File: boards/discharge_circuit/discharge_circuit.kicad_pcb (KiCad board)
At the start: 2 copper layers, 93 x 43.5 mm, 11 parts, among them J1 Unfused TS, J2 Shutdown Circuit, J3 TSMP/TSAL, K1 G2RL-1-E

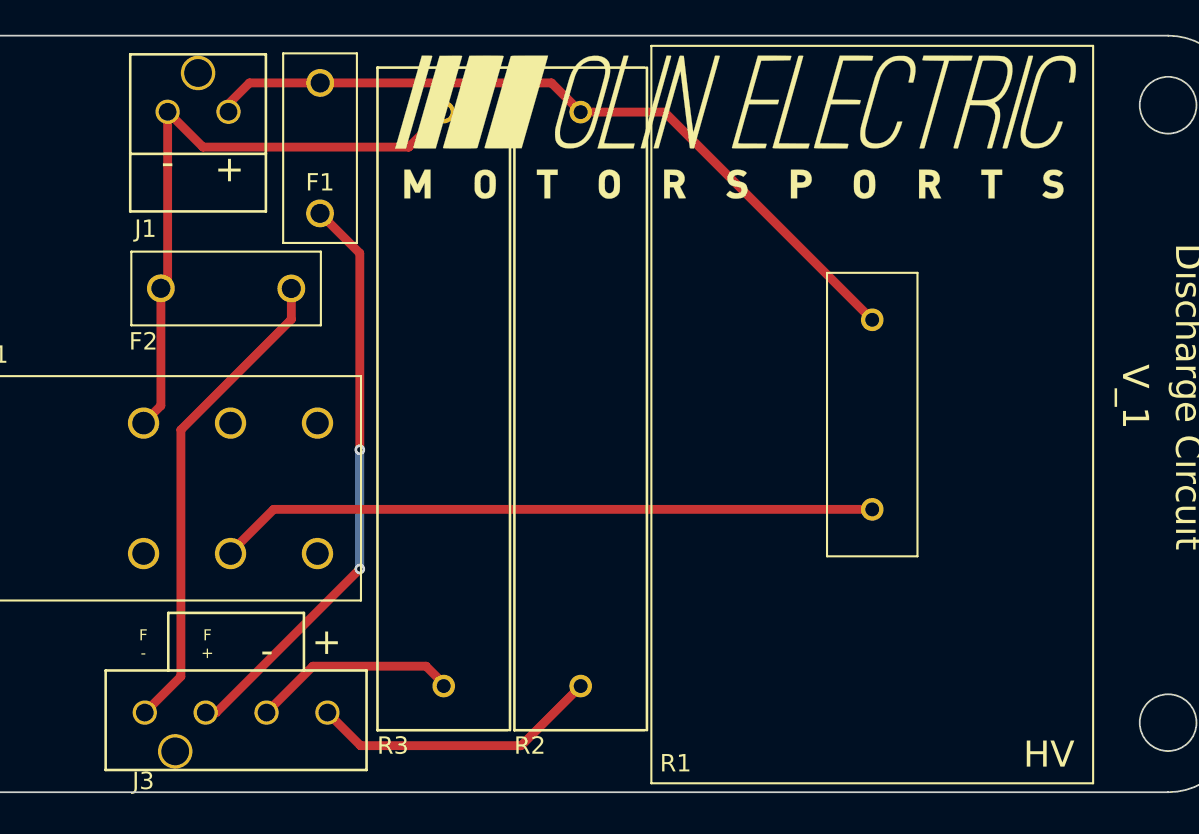
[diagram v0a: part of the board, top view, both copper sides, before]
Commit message: modifying discharge circuit to fit in accumulator
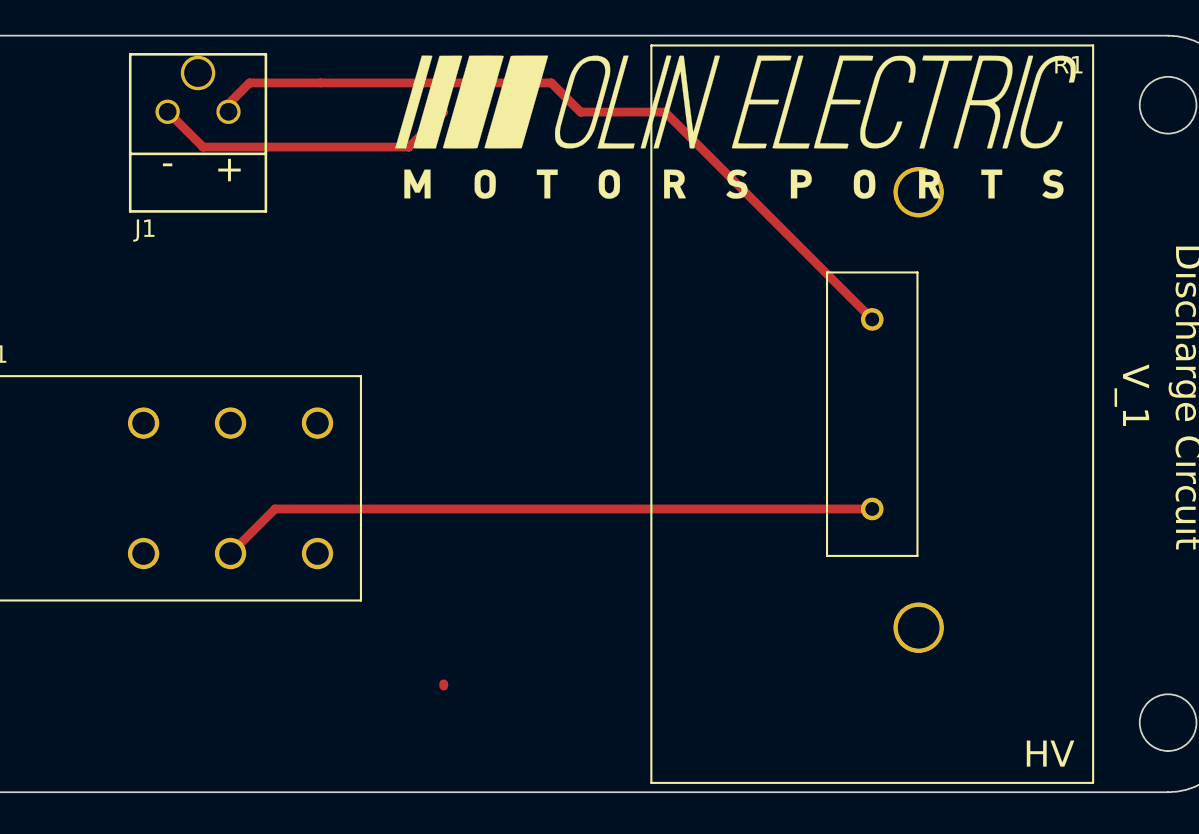
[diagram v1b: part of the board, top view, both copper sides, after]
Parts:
- removed F1, F2: F_3.15A_450V, footprints:Fuse_TE7_Littelfuse-807Series
- removed J3: TSMP/TSAL, footprints:Ultrafit_4
- removed R2, R3: R_10k_HV, footprints:R_10K_HV
- moved R1 10.9 mm to (174.0, 99.6), turned to 270 degrees
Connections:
- R1 pad 1: Net-(K1-Pad6) -> /TS+Unfused
- R1 pad 2: /TS+Unfused -> Net-(K1-Pad6)
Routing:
- net /TS+Fused: track 33.7 -> 0.00 mm, vias 2 -> 0
- net /TS-Fused: track 27.9 -> 0.00 mm
- net /TS-Unfused: track 36.6 -> 17.6 mm
- net Net-(J3-Pad4): track 16.8 -> 0.00 mm
- net Net-(J3-Pad3): track 11.8 -> 0.00 mm
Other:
- board text removed: "F +"
- board text removed: "F -"

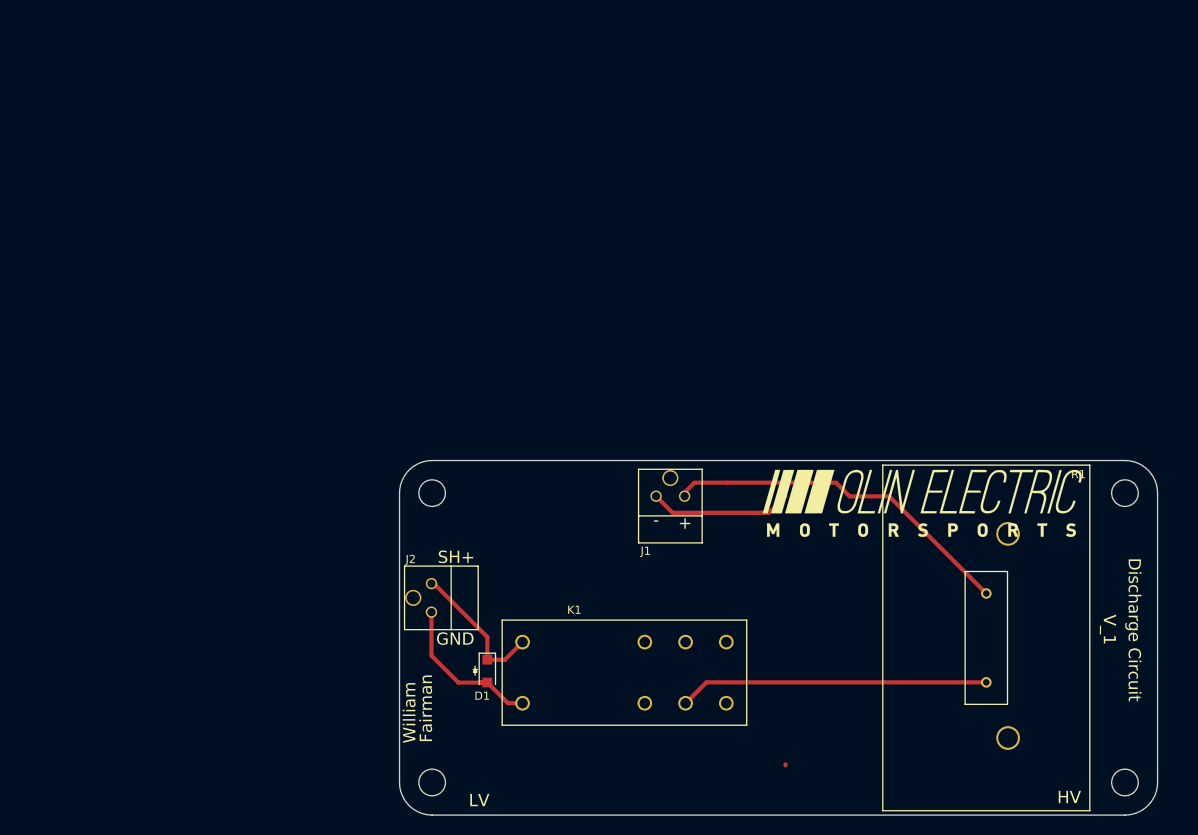
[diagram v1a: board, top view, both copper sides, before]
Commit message: restored older version of discharge circuit and added additional connectors
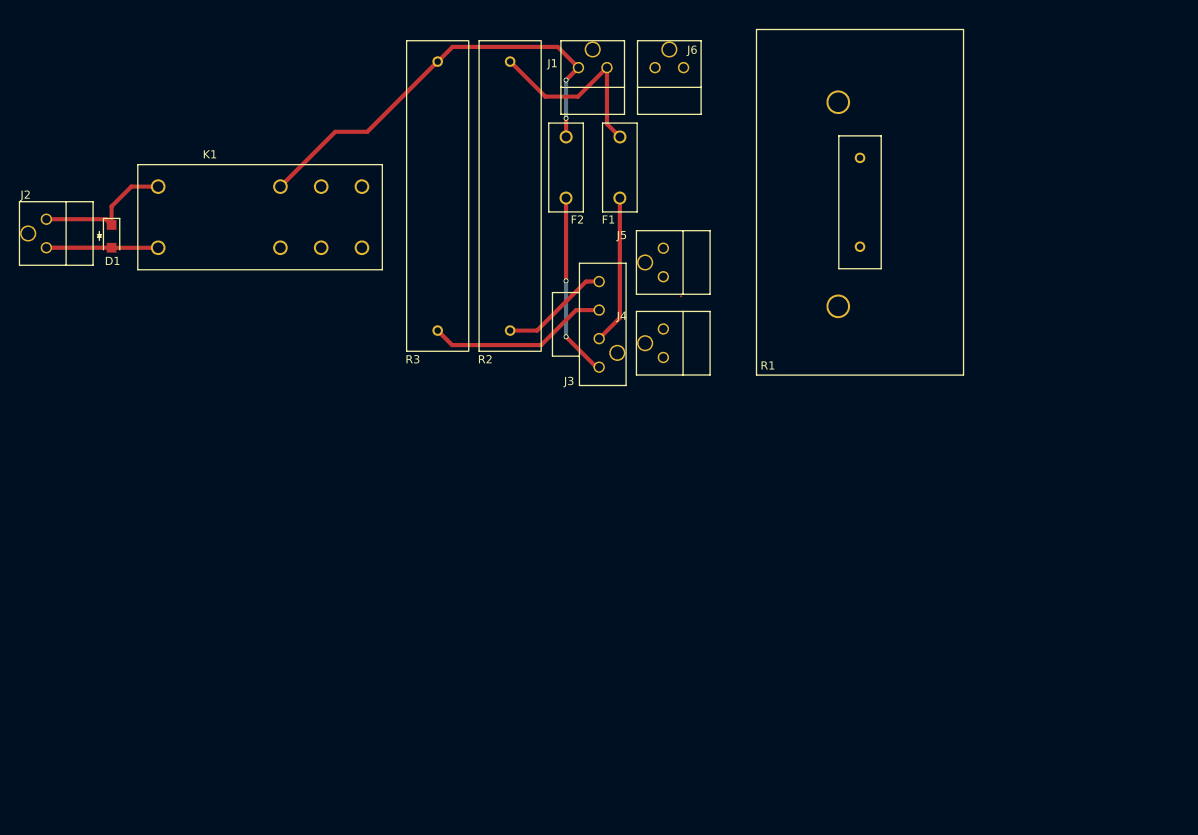
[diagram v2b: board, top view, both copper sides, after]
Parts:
- removed G***: LOGO, footprints:Logo_Large
- added F1: F_3.15A_450V, footprints:Fuse_TE7_Littelfuse-807Series, F.Cu at (129.0, 51.1)
- added F2: F_3.15A_450V, footprints:Fuse_TE7_Littelfuse-807Series, F.Cu at (122.4, 51.1)
- added J3: TSMP, footprints:Ultrafit_4, F.Cu at (126.5, 66.5)
- added J4: TSAL, footprints:Ultrafit_2, F.Cu at (134.4, 70.6)
- added J5: IMD, footprints:Ultrafit_2, F.Cu at (134.4, 60.7)
- added J6: EM/Precharge, footprints:Ultrafit_2, F.Cu at (133.3, 35.1)
- added R2: R_10k_HV, footprints:R_10K_HV, F.Cu at (115.6, 67.3)
- added R3: R_10k_HV, footprints:R_10K_HV, F.Cu at (106.7, 67.3)
- moved K1 71.6 mm to (72.4, 57.1)
- moved D1 70.5 mm to (66.7, 55.8)
- moved J2 65.0 mm to (58.7, 57.1)
- moved J1 53.4 mm to (124.0, 35.1)
- moved R1 45.3 mm to (158.5, 57.0), turned to 90 degrees
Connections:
- R1 pad 1: /TS+Unfused -> Net-(K1-Pad6)
- R1 pad 2: Net-(K1-Pad6) -> /TS+Unfused
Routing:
- net Net-(K1-Pad6): track 38.0 -> 0.00 mm
- net /TS-Unfused: track 17.6 -> 53.9 mm, vias 0 -> 2
- net Net-(J3-Pad3): track 0.00 -> 19.8 mm
- net /TS+Unfused: track 43.8 -> 24.3 mm
- net /TS-Fused: track 0.00 -> 17.0 mm, vias 0 -> 2
- net /TS+Fused: track 0.00 -> 14.7 mm
- net Net-(J3-Pad4): track 0.00 -> 10.1 mm
- net Net-(J3-Pad1): track 0.00 -> 8.91 mm
- net Net-(J3-Pad2): track 0.00 -> 6.11 mm
- net GND: track 19.7 -> 13.7 mm
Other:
- board outline removed
- net class Default: clearance 0.1016 -> 0.0508; via_dia 0.6096 -> 0.6; via_drill 0.3048 -> 0.4
- rule trace_clearance: 0.1016 -> 0.0508
- rule via_min_drill: 0.3048 -> 0.3
- rule via_min_size: 0.6096 -> 0.4
- board text removed: "+"
- board text removed: "-"
- board text removed: "Discharge Circuit"
- board text removed: "Fairman"
- board text removed: "GND"
- board text removed: "HV"
- board text removed: "LV"
- board text removed: "SH+"
- board text removed: "V_1"
- board text removed: "William"

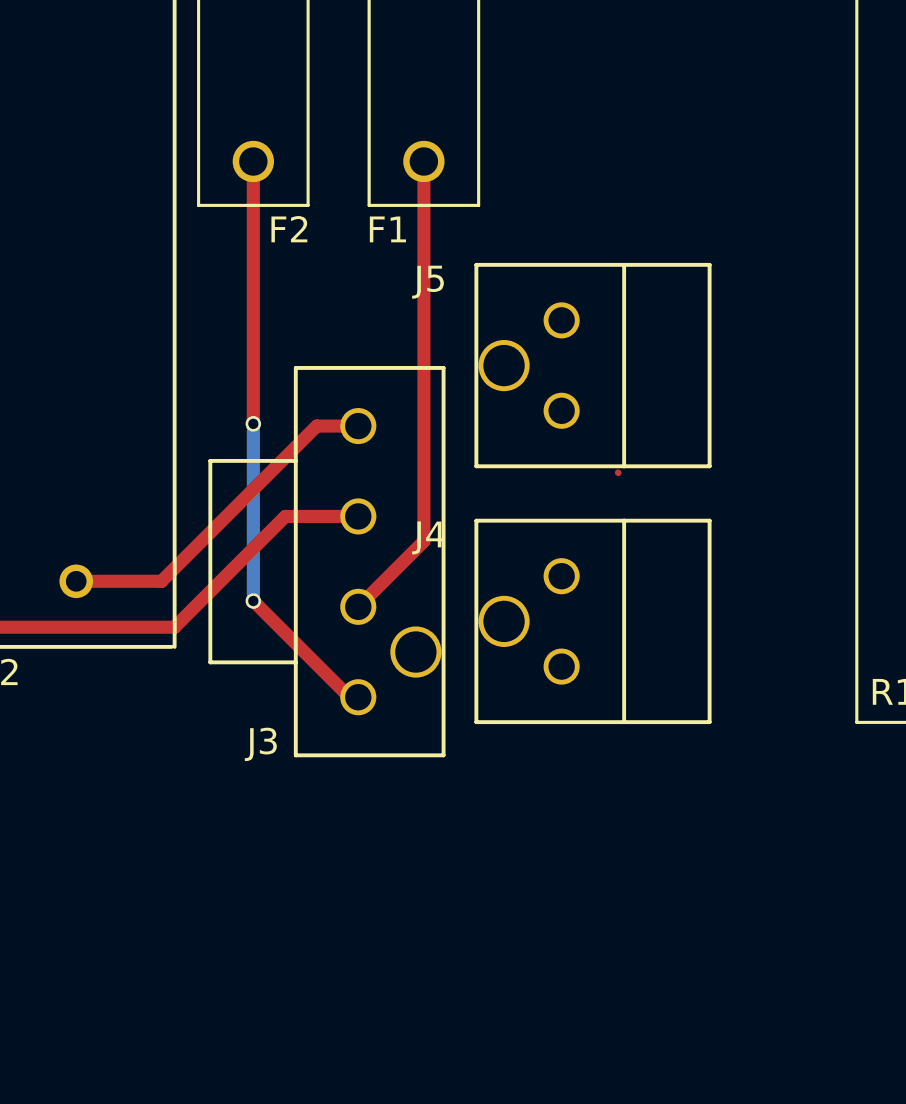
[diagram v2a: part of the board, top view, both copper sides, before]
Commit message: modified discharge circuit
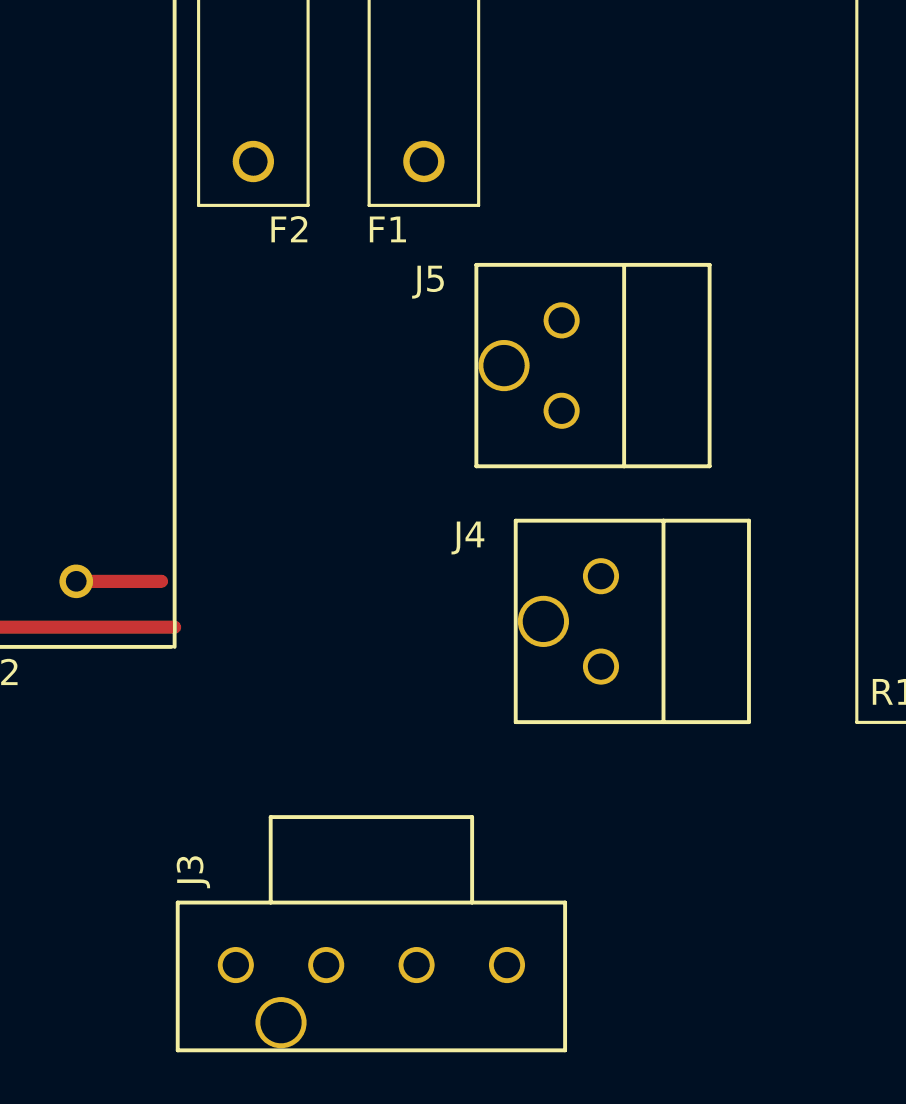
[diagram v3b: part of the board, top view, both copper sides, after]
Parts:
- moved J3 15.6 mm to (127.0, 82.2), turned to 270 degrees
- moved J4 1.52 mm to (135.9, 70.6)
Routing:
- net Net-(J3-Pad3): track 19.8 -> 0.00 mm
- net /TS-Fused: track 17.0 -> 0.00 mm, vias 2 -> 0
- net /TS+Fused: track 14.7 -> 0.00 mm
- net Net-(J3-Pad4): track 10.1 -> 0.00 mm
- net Net-(J3-Pad2): track 6.11 -> 13.4 mm
- net Net-(J3-Pad1): track 8.91 -> 3.30 mm
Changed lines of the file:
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@@
     (thickness 1.6)
     (drawings 1)
-    (tracks 45)
+    (tracks 32)
     (zones 0)
     (modules 13)
@@
   )
   (module footprints:Ultrafit_4 (layer F.Cu)
-    (at 126.492 66.548)
-    (fp_text reference J3 (at -3.683 6.985) (layer F.SilkS)
-      (effects (font (size 1 1) (thickness 0.15)))
-    )
-    (fp_text value TSMP (at 4.572 0.508 90) (layer F.Fab) hide
+    (at 127 82.169 270)
+    (fp_text reference J3 (at -3.683 6.985 270) (layer F.SilkS)
+      (effects (font (size 1 1) (thickness 0.15)))
+    )
+    (fp_text value TSMP (at 4.572 0.508 360) (layer F.Fab) hide
       (effects (font (size 1 1) (thickness 0.15)))
     )
@@
     (fp_line (start -2.54 3.81) (end -5.588 3.81) (layer F.Fab) (width 0.15))
     (fp_line (start -5.588 3.81) (end -5.588 -3.81) (layer F.Fab) (width 0.15))
-    (fp_text user "6.55mm Clearance" (at -4.07 0 90) (layer F.Fab)
+    (fp_text user "6.55mm Clearance" (at -4.07 0 360) (layer F.Fab)
       (effects (font (size 0.5 0.5) (thickness 0.08)))
     )
@@
     (fp_line (start -2.42 7.5) (end -2.42 -7.5) (layer F.SilkS) (width 0.15))
     (fp_line (start 3.302 7.5) (end 3.302 -7.5) (layer F.SilkS) (width 0.15))
-    (pad 2 thru_hole circle (at 0 1.75) (size 1.397 1.397) (drill 1.02) (layers *.Cu *.Mask)
+    (pad 2 thru_hole circle (at 0 1.75 270) (size 1.397 1.397) (drill 1.02) (layers *.Cu *.Mask)
       (net 11 "Net-(J3-Pad2)"))
-    (pad 1 thru_hole circle (at 0 5.25) (size 1.397 1.397) (drill 1.02) (layers *.Cu *.Mask)
+    (pad 1 thru_hole circle (at 0 5.25 270) (size 1.397 1.397) (drill 1.02) (layers *.Cu *.Mask)
       (net 12 "Net-(J3-Pad1)"))
-    (pad "" thru_hole circle (at 2.23 3.5) (size 1.981 1.981) (drill 1.6) (layers *.Cu *.Mask))
-    (pad 3 thru_hole circle (at 0 -1.75 180) (size 1.397 1.397) (drill 1.02) (layers *.Cu *.Mask)
+    (pad "" thru_hole circle (at 2.23 3.5 270) (size 1.981 1.981) (drill 1.6) (layers *.Cu *.Mask))
+    (pad 3 thru_hole circle (at 0 -1.75 90) (size 1.397 1.397) (drill 1.02) (layers *.Cu *.Mask)
       (net 7 "Net-(J3-Pad3)"))
-    (pad 4 thru_hole circle (at 0 -5.25 180) (size 1.397 1.397) (drill 1.02) (layers *.Cu *.Mask)
+    (pad 4 thru_hole circle (at 0 -5.25 90) (size 1.397 1.397) (drill 1.02) (layers *.Cu *.Mask)
       (net 8 "Net-(J3-Pad4)"))
   )
@@
   )
   (module footprints:Ultrafit_2 (layer F.Cu)
-    (at 134.366 70.612 180)
+    (at 135.89 70.612 180)
     (fp_text reference J4 (at 5.08 5.08 180) (layer F.SilkS)
       (effects (font (size 1 1) (thickness 0.15)))
@@
     (arrow2b (pts (xy 72.39 43.307) (xy 73.516504 42.720579)))
   )
-  (segment (start 136.55 63.1016) (end 136.5604 63.112) (width 0.25) (layer F.Cu) (net 0))
   (segment (start 66.675 54.353) (end 66.675 52.07) (width 0.508) (layer F.Cu) (net 1))
   (segment (start 69.095 49.65) (end 72.39 49.65) (width 0.508) (layer F.Cu) (net 1))
@@
   (segment (start 58.674 57.15) (end 66.672 57.15) (width 0.508) (layer F.Cu) (net 2))
   (segment (start 66.672 57.15) (end 66.675 57.153) (width 0.508) (layer F.Cu) (net 2))
-  (segment (start 129.032 51.054) (end 129.032 65.758) (width 0.508) (layer F.Cu) (net 3))
   (segment (start 127.452 35.052) (end 127.452 41.964) (width 0.508) (layer F.Cu) (net 4))
   (segment (start 127.452 41.964) (end 129.042 43.554) (width 0.508) (layer F.Cu) (net 4))
@@
   (segment (start 119.888 38.608) (end 123.896 38.608) (width 0.508) (layer F.Cu) (net 4))
   (segment (start 123.896 38.608) (end 127.452 35.052) (width 0.508) (layer F.Cu) (net 4))
-  (segment (start 122.428 51.054) (end 122.428 61.214) (width 0.508) (layer F.Cu) (net 5))
-  (via (at 122.428 61.214) (size 0.6) (drill 0.4) (layers F.Cu B.Cu) (net 5))
-  (segment (start 122.428 61.214) (end 122.428 68.072) (width 0.508) (layer B.Cu) (net 5))
-  (via (at 122.428 68.072) (size 0.6) (drill 0.4) (layers F.Cu B.Cu) (net 5))
   (segment (start 123.952 35.052) (end 122.428 36.576) (width 0.508) (layer F.Cu) (net 6))
   (segment (start 122.438 41.285) (end 122.438 43.554) (width 0.508) (layer F.Cu) (net 6))
@@
   (segment (start 108.498 32.512) (end 121.412 32.512) (width 0.508) (layer F.Cu) (net 6))
   (segment (start 121.412 32.512) (end 123.952 35.052) (width 0.508) (layer F.Cu) (net 6))
-  (segment (start 126.492 64.798) (end 123.67 64.798) (width 0.508) (layer F.Cu) (net 7))
-  (segment (start 123.67 64.798) (end 119.38 69.088) (width 0.508) (layer F.Cu) (net 7))
-  (segment (start 119.38 69.088) (end 108.458 69.088) (width 0.508) (layer F.Cu) (net 7))
-  (segment (start 126.492 61.298) (end 124.884 61.298) (width 0.508) (layer F.Cu) (net 8))
-  (segment (start 124.884 61.298) (end 118.872 67.31) (width 0.508) (layer F.Cu) (net 8))
-  (segment (start 129.032 65.758) (end 126.492 68.298) (width 0.508) (layer F.Cu) (net 11))
+  (segment (start 119.38 69.088) (end 108.458 69.088) (width 0.508) (layer F.Cu) (net 11))
   (segment (start 108.458 69.088) (end 106.68 67.31) (width 0.508) (layer F.Cu) (net 11))
-  (segment (start 122.428 68.072) (end 126.154 71.798) (width 0.508) (layer F.Cu) (net 12))
-  (segment (start 126.154 71.798) (end 126.492 71.798) (width 0.508) (layer F.Cu) (net 12))
   (segment (start 118.872 67.31) (end 115.57 67.31) (width 0.508) (layer F.Cu) (net 12))
 )
